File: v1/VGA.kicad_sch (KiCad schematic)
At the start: 28 parts, among them J10 DB15_Female_HighDensity_Mount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, J9 Conn_02x06_Odd_Even

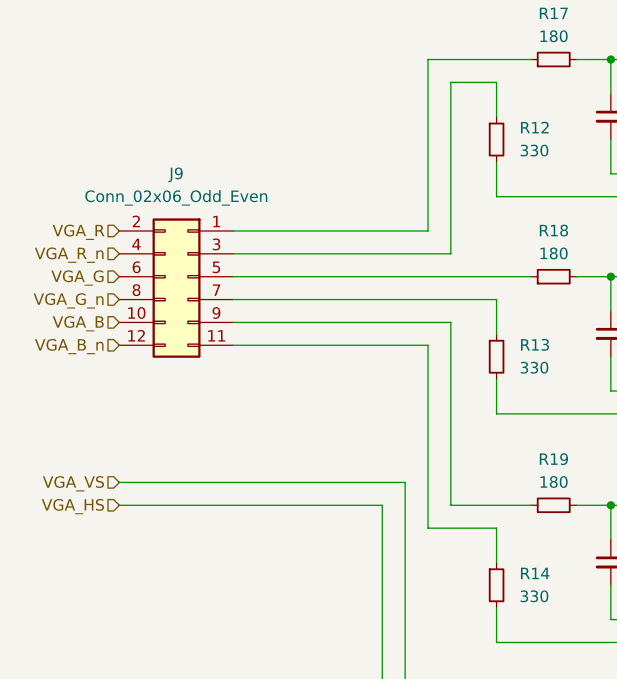
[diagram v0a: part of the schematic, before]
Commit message: Updated VGA jumper block from 2x6 to 3x6
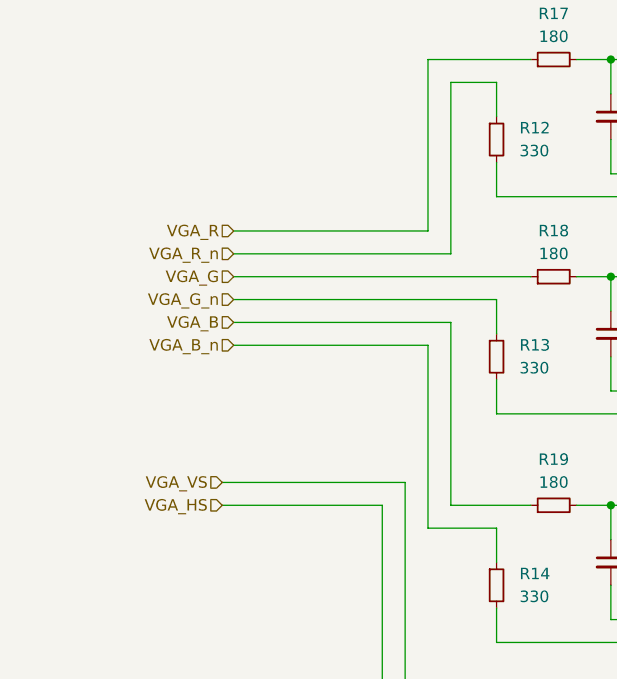
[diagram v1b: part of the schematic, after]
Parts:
- removed J9: Conn_02x06_Odd_Even, Connector_PinHeader_2.54mm:PinHeader_2x06_P2.54mm_Vertical, symbol Connector_Generic:Conn_02x06_Odd_Even
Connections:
- net VGA_B: now also R19.1
- net VGA_B_n: now also R14.1
- net VGA_G: now also R18.1
- net VGA_G_n: now also R13.1
- net VGA_R: now also R17.1
- net VGA_R_n: now also R12.1
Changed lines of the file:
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@@
     (stroke (width 0) (type default) (color 0 0 0 0))
   )
-  (wire (pts (xy 27.94 113.03) (xy 57.15 113.03))
+  (wire (pts (xy 39.37 113.03) (xy 57.15 113.03))
     (stroke (width 0) (type default) (color 0 0 0 0))
   )
@@
     (stroke (width 0) (type default) (color 0 0 0 0))
   )
-  (wire (pts (xy 27.94 110.49) (xy 59.69 110.49))
+  (wire (pts (xy 39.37 110.49) (xy 59.69 110.49))
     (stroke (width 0) (type default) (color 0 0 0 0))
   )
@@
     (stroke (width 0) (type default) (color 0 0 0 0))
   )
-  (hierarchical_label "VGA_VS" (shape input) (at 27.94 110.49 180)
-    (effects (font (size 1.27 1.27)) (justify right))
-  )
-  (hierarchical_label "VGA_R_n" (shape input) (at 27.94 85.09 180)
-    (effects (font (size 1.27 1.27)) (justify right))
-  )
-  (hierarchical_label "VGA_B_n" (shape input) (at 27.94 95.25 180)
-    (effects (font (size 1.27 1.27)) (justify right))
-  )
-  (hierarchical_label "VGA_R" (shape input) (at 27.94 82.55 180)
-    (effects (font (size 1.27 1.27)) (justify right))
-  )
-  (hierarchical_label "VGA_G_n" (shape input) (at 27.94 90.17 180)
-    (effects (font (size 1.27 1.27)) (justify right))
-  )
-  (hierarchical_label "VGA_G" (shape input) (at 27.94 87.63 180)
-    (effects (font (size 1.27 1.27)) (justify right))
-  )
-  (hierarchical_label "VGA_B" (shape input) (at 27.94 92.71 180)
-    (effects (font (size 1.27 1.27)) (justify right))
-  )
-  (hierarchical_label "VGA_HS" (shape input) (at 27.94 113.03 180)
+  (hierarchical_label "VGA_VS" (shape input) (at 39.37 110.49 180)
+    (effects (font (size 1.27 1.27)) (justify right))
+  )
+  (hierarchical_label "VGA_R_n" (shape input) (at 40.64 85.09 180)
+    (effects (font (size 1.27 1.27)) (justify right))
+  )
+  (hierarchical_label "VGA_B_n" (shape input) (at 40.64 95.25 180)
+    (effects (font (size 1.27 1.27)) (justify right))
+  )
+  (hierarchical_label "VGA_R" (shape input) (at 40.64 82.55 180)
+    (effects (font (size 1.27 1.27)) (justify right))
+  )
+  (hierarchical_label "VGA_G_n" (shape input) (at 40.64 90.17 180)
+    (effects (font (size 1.27 1.27)) (justify right))
+  )
+  (hierarchical_label "VGA_G" (shape input) (at 40.64 87.63 180)
+    (effects (font (size 1.27 1.27)) (justify right))
+  )
+  (hierarchical_label "VGA_B" (shape input) (at 40.64 92.71 180)
+    (effects (font (size 1.27 1.27)) (justify right))
+  )
+  (hierarchical_label "VGA_HS" (shape input) (at 39.37 113.03 180)
     (effects (font (size 1.27 1.27)) (justify right))
   )
@@
     (pin "2")
   )
-  (symbol (lib_id "Connector_Generic:Conn_02x06_Odd_Even") (at 35.56 87.63 0) (mirror y) (unit 1)
-    (in_bom yes) (on_board yes) (fields_autoplaced)
-    (property "Reference" "J9" (id 0) (at 34.29 76.2 0))
-    (property "Value" "Conn_02x06_Odd_Even" (id 1) (at 34.29 78.74 0))
-    (property "Footprint" "Connector_PinHeader_2.54mm:PinHeader_2x06_P2.54mm_Vertical" (id 2) (at 35.56 87.63 0)
-      (effects (font (size 1.27 1.27)) hide)
-    )
-    (property "Datasheet" "~" (id 3) (at 35.56 87.63 0)
-      (effects (font (size 1.27 1.27)) hide)
-    )
-    (pin "1")
-    (pin "10")
-    (pin "11")
-    (pin "12")
-    (pin "2")
-    (pin "3")
-    (pin "4")
-    (pin "5")
-    (pin "6")
-    (pin "7")
-    (pin "8")
-    (pin "9")
-  )
   (symbol (lib_id "Device:R_Small") (at 69.85 121.92 0) (unit 1)

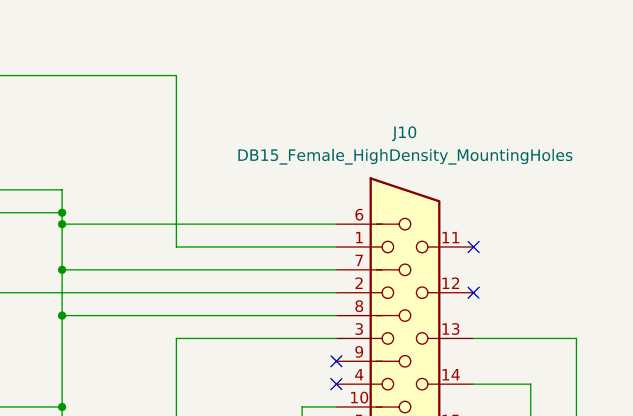
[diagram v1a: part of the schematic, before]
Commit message: Updated VGA jumper block from 3x6 to 3x8
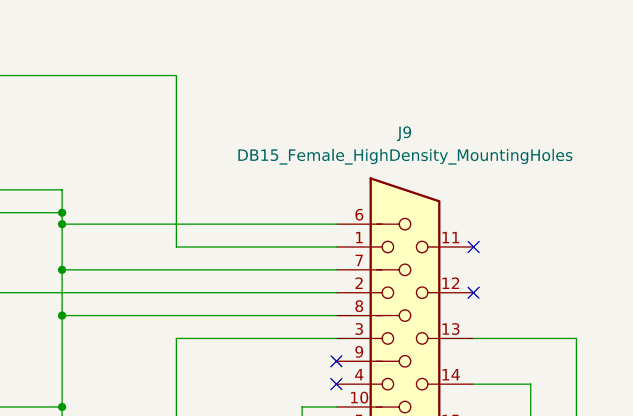
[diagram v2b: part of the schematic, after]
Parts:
- renumbered J10 to J9
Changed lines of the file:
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@@
   (symbol (lib_id "Connector:DB15_Female_HighDensity_MountingHoles") (at 177.8 92.71 0) (unit 1)
     (in_bom yes) (on_board yes) (fields_autoplaced)
-    (property "Reference" "J10" (id 0) (at 177.8 69.85 0))
+    (property "Reference" "J9" (id 0) (at 177.8 69.85 0))
     (property "Value" "DB15_Female_HighDensity_MountingHoles" (id 1) (at 177.8 72.39 0))
     (property "Footprint" "TangNano20k:DSUB-15-HD_Female_Horizontal_P2.29x1.98mm_EdgePinOffset8.35mm_Housed_MountingHolesOffset10.89mm" (id 2) (at 153.67 82.55 0)
